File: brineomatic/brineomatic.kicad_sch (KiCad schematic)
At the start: 7 parts, among them U1 ESP32-S3-DEVKITC

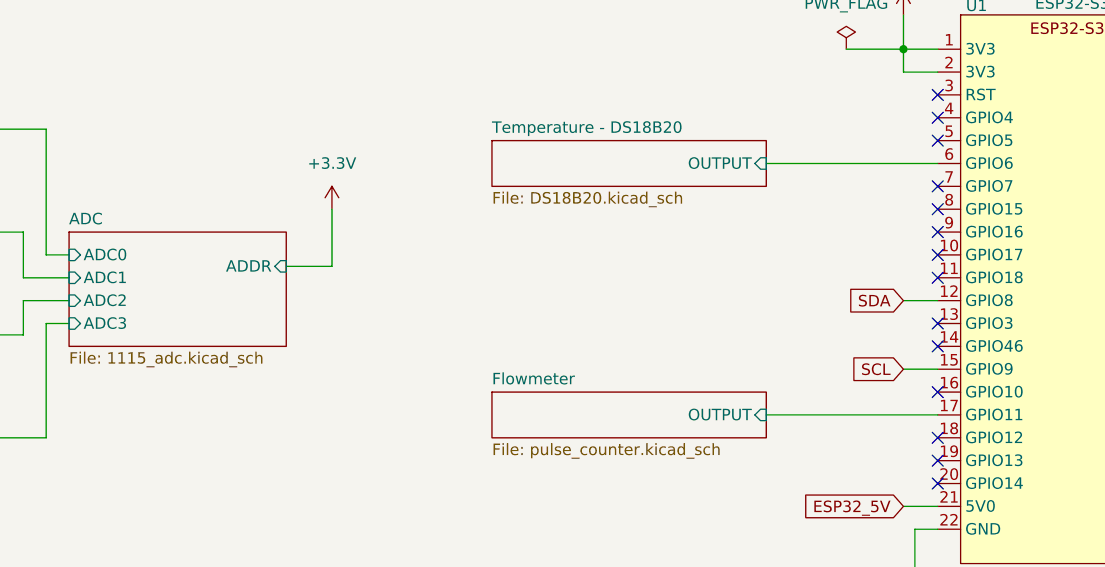
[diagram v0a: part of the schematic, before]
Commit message: added alert line to adc
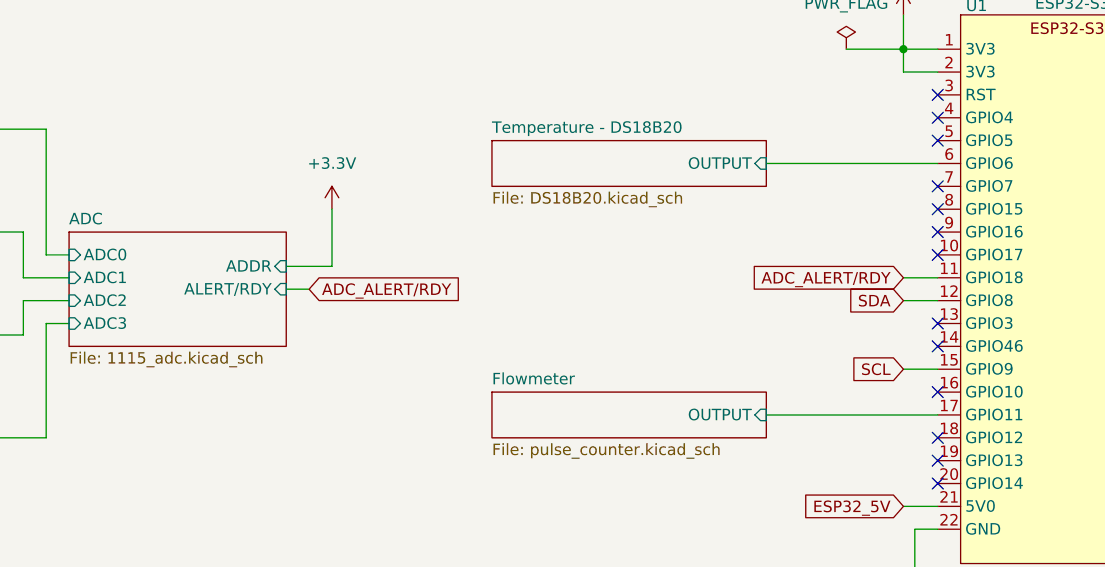
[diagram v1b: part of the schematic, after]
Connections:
- net ADC_ALERT/RDY: now reaches U1.11 (GPIO18)
- no-connect marks 25 -> 24
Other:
- sheet ADC ports: added ALERT/RDY; removed none
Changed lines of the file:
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@@
-	)
-	(no_connect
-		(at 161.29 76.2)
 	)
 	(no_connect
@@
 	(wire
 		(pts
+			(xy 88.9 77.47) (xy 91.44 77.47)
+		)
+		(stroke
+			(width 0)
+			(type default)
+		)
+	)
+	(wire
+		(pts
 			(xy 199.39 68.58) (xy 222.25 68.58)
 		)
@@
 	(wire
 		(pts
+			(xy 157.48 76.2) (xy 161.29 76.2)
+		)
+		(stroke
+			(width 0)
+			(type default)
+		)
+	)
+	(wire
+		(pts
 			(xy 207.01 50.8) (xy 207.01 52.07)
 		)
@@
 			(width 0)
 			(type default)
+		)
+	)
+	(global_label "ADC_ALERT{slash}RDY"
+		(shape input)
+		(at 157.48 76.2 180)
+		(fields_autoplaced yes)
+		(effects
+			(font
+				(size 1.27 1.27)
+			)
+			(justify right)
+		)
+		(property "Intersheetrefs" "${INTERSHEET_REFS}"
+			(at 139.4362 76.2 0)
+			(effects
+				(font
+					(size 1.27 1.27)
+				)
+				(justify right)
+				(hide yes)
+			)
 		)
 	)
@@
 				)
 				(justify right)
+				(hide yes)
+			)
+		)
+	)
+	(global_label "ADC_ALERT{slash}RDY"
+		(shape input)
+		(at 91.44 77.47 0)
+		(fields_autoplaced yes)
+		(effects
+			(font
+				(size 1.27 1.27)
+			)
+			(justify left)
+		)
+		(property "Intersheetrefs" "${INTERSHEET_REFS}"
+			(at 109.4838 77.47 0)
+			(effects
+				(font
+					(size 1.27 1.27)
+				)
+				(justify left)
 				(hide yes)
 			)
@@
 			(effects
 				(font
+					(size 1.27 1.27)
+				)
+				(justify right)
+			)
+		)
+		(pin "ALERT{slash}RDY" input
+			(at 88.9 77.47 0)
+			(effects
+				(font

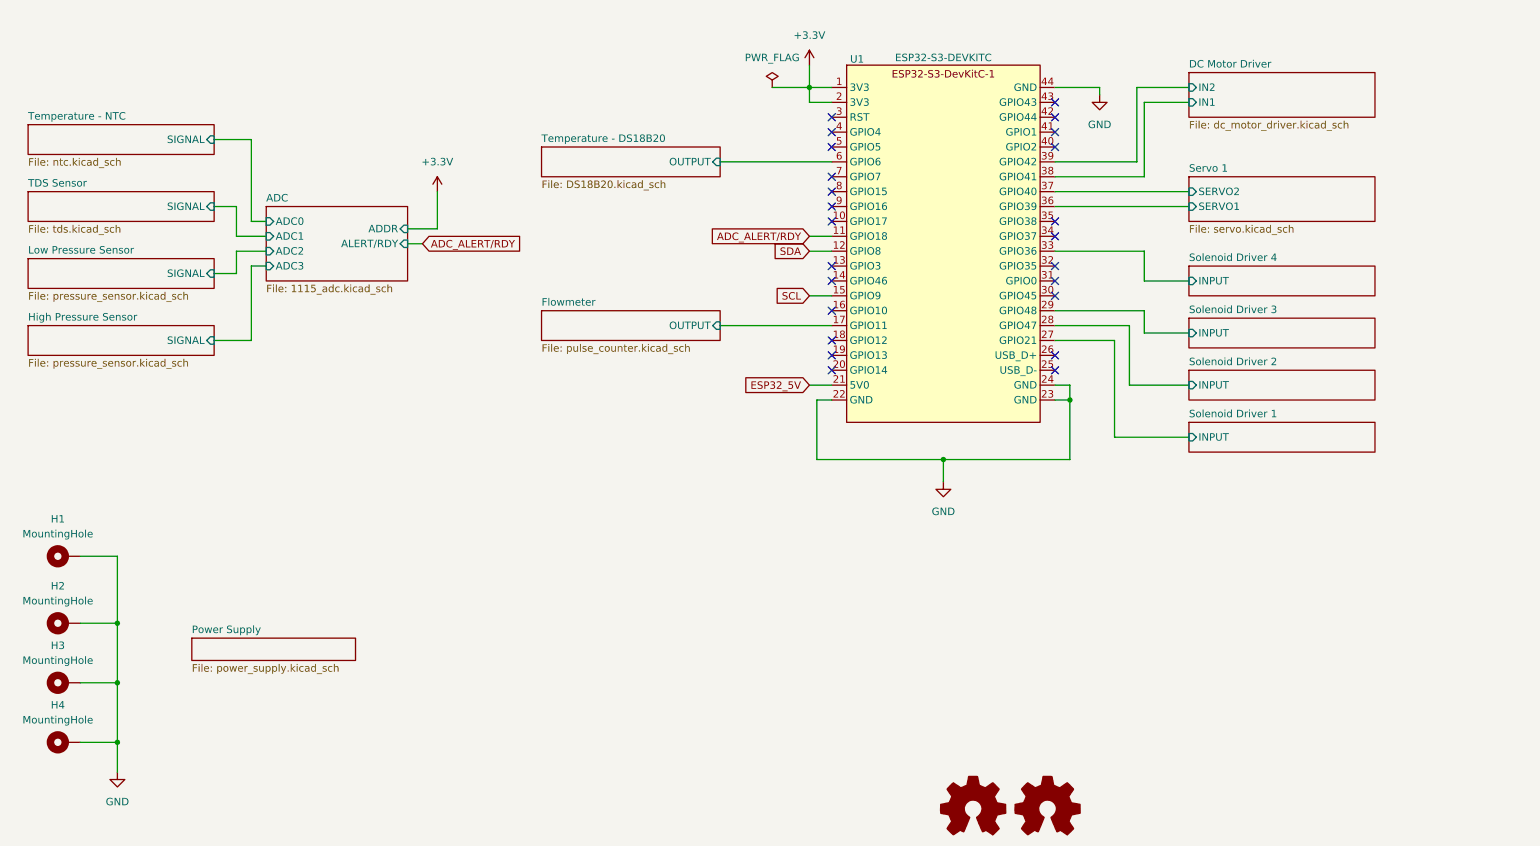
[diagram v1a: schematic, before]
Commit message: added piezo buzzer
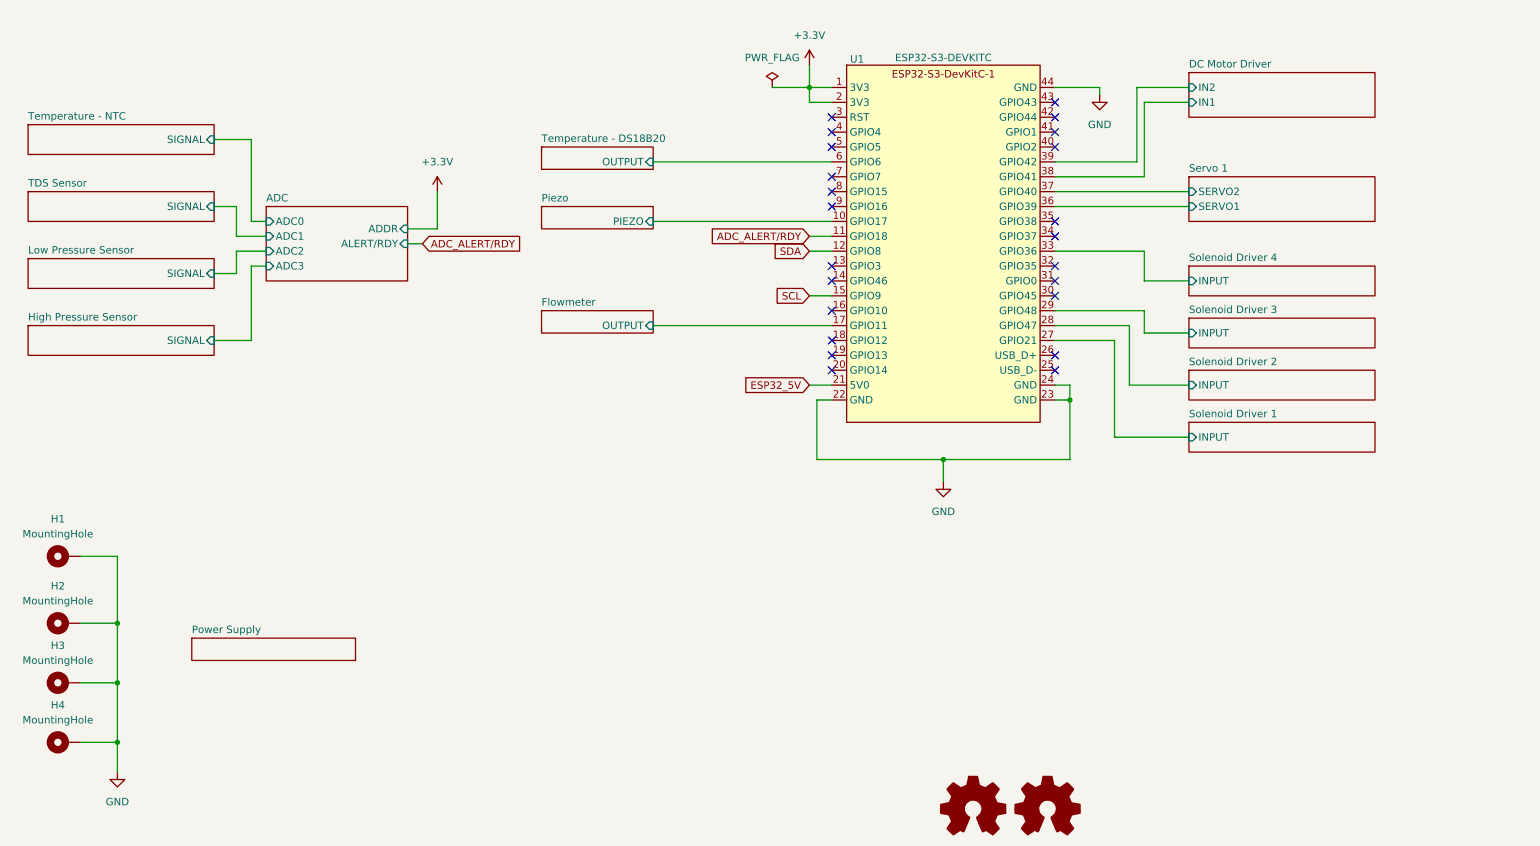
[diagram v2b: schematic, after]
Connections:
- net Piezo/PIEZO: now reaches U1.10 (GPIO17)
- no-connect marks 24 -> 23
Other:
- added sheet Piezo (piezo.kicad_sch)
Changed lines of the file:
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@@
-	)
-	(no_connect
-		(at 161.29 73.66)
 	)
 	(no_connect
@@
 	(wire
 		(pts
+			(xy 130.81 63.5) (xy 161.29 63.5)
+		)
+		(stroke
+			(width 0)
+			(type default)
+		)
+	)
+	(wire
+		(pts
 			(xy 39.37 162.56) (xy 39.37 167.64)
 		)
@@
 	(wire
 		(pts
-			(xy 161.29 91.44) (xy 142.24 91.44)
-		)
-		(stroke
-			(width 0)
-			(type default)
-		)
-	)
-	(wire
-		(pts
 			(xy 158.75 114.3) (xy 180.34 114.3)
 		)
@@
 	(wire
 		(pts
+			(xy 130.81 73.66) (xy 161.29 73.66)
+		)
+		(stroke
+			(width 0)
+			(type default)
+		)
+	)
+	(wire
+		(pts
 			(xy 180.34 118.11) (xy 180.34 114.3)
 		)
@@
 	(wire
 		(pts
-			(xy 142.24 63.5) (xy 161.29 63.5)
-		)
-		(stroke
-			(width 0)
-			(type default)
-		)
-	)
-	(wire
-		(pts
 			(xy 157.48 50.8) (xy 157.48 53.34)
 		)
@@
 		(pts
 			(xy 180.34 114.3) (xy 201.93 114.3)
+		)
+		(stroke
+			(width 0)
+			(type default)
+		)
+	)
+	(wire
+		(pts
+			(xy 130.81 91.44) (xy 161.29 91.44)
 		)
 		(stroke
@@
 				)
 				(justify left top)
+				(hide yes)
 			)
 		)
@@
 				)
 				(justify left top)
+				(hide yes)
 			)
 		)
@@
 				)
 				(justify left top)
+				(hide yes)
 			)
 		)
@@
 				)
 				(justify left top)
+				(hide yes)
 			)
 		)
@@
 				)
 				(justify left top)
+				(hide yes)
 			)
 		)
@@
 	(sheet
 		(at 111.76 60.96)
-		(size 30.48 5.08)
+		(size 19.05 3.81)
 		(fields_autoplaced yes)
 		(stroke
@@
 		)
 		(property "Sheetfile" "DS18B20.kicad_sch"
-			(at 111.76 66.6246 0)
+			(at 111.76 65.3546 0)
 			(effects
 				(font
@@
 				)
 				(justify left top)
+				(hide yes)
 			)
 		)
 		(pin "OUTPUT" input
-			(at 142.24 63.5 0)
+			(at 130.81 63.5 0)
 			(effects
 				(font
@@
 				(path "/96477ae2-ef08-48f3-8dd4-fe4478541f68"
 					(page "4")
+				)
+			)
+		)
+	)
+	(sheet
+		(at 111.76 71.12)
+		(size 19.05 3.81)
+		(fields_autoplaced yes)
+		(stroke
+			(width 0.1524)
+			(type solid)
+		)
+		(fill
+			(color 0 0 0 0.0000)
+		)
+		(property "Sheetname" "Piezo"
+			(at 111.76 70.4084 0)
+			(effects
+				(font
+					(size 1.27 1.27)
+				)
+				(justify left bottom)
+			)
+		)
+		(property "Sheetfile" "piezo.kicad_sch"
+			(at 111.76 75.5146 0)
+			(effects
+				(font
+					(size 1.27 1.27)
+				)
+				(justify left top)
+				(hide yes)
+			)
+		)
+		(pin "PIEZO" input
+			(at 130.81 73.66 0)
+			(effects
+				(font
+					(size 1.27 1.27)
+				)
+				(justify right)
+			)
+		)
+		(instances
+			(project "brineomatic"
+				(path "/96477ae2-ef08-48f3-8dd4-fe4478541f68"
+					(page "16")
 				)
 			)
@@
 				)
 				(justify left top)
+				(hide yes)
 			)
 		)
@@
 	(sheet
 		(at 111.76 88.9)
-		(size 30.48 5.08)
+		(size 19.05 3.81)
 		(fields_autoplaced yes)
 		(stroke
@@
 		)
 		(property "Sheetfile" "pulse_counter.kicad_sch"
-			(at 111.76 94.5646 0)
+			(at 111.76 93.2946 0)
 			(effects
 				(font
@@
 				)
 				(justify left top)
+				(hide yes)
 			)
 		)
 		(pin "OUTPUT" input
-			(at 142.24 91.44 0)
+			(at 130.81 91.44 0)
 			(effects
 				(font
@@
 				)
 				(justify left top)
+				(hide yes)
 			)
 		)
@@
 				)
 				(justify left top)
-			)
-		)
+				(hide yes)
+			)
+		)

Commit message: did a bunch of schematic work for Rev B
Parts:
- added R17, R19: 10k, symbol Device:R_Small_US
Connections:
- net +3.3V: now also R17.2
- net GND: now also R19.2
- net Servos/SERVO1: now also U1.34 (GPIO37); no longer U1.36 (GPIO39)
- net Servos/SERVO2: now also U1.36 (GPIO39); no longer U1.37 (GPIO40)
- net Brine Flowmeter/OUTPUT: now reaches U1.18 (GPIO12)
- net Stepper Driver/DIR: now reaches U1.40 (GPIO2)
- net Stepper Driver/STEP: now reaches U1.41 (GPIO1)
- net DC Motor Driver/IN1 renamed Stepper Driver/RX
- net DC Motor Driver/IN2 renamed Stepper Driver/EN
- new net Stepper Driver/MS1: R17.1
- new net Stepper Driver/MS2: R19.1
- new net Stepper Driver/TX: U1.37 (GPIO40)
- no-connect marks 23 -> 19
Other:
- sheet Flowmeter renamed Product Flowmeter
- sheet Servo 1 renamed Servos
- sheet TDS Sensor renamed Product TDS
- removed sheet DC Motor Driver
- removed sheet Temperature - NTC
- added sheet Brine Flowmeter (pulse_counter.kicad_sch)
- added sheet Brine TDS (tds.kicad_sch)
- added sheet Stepper Driver (tmc2209.kicad_sch)

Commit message: worked on schematic and layout a bit more.
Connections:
- net Stepper Driver/TX is gone; now on net Stepper Driver/RX: U1.37 (GPIO40)
- net Stepper Driver/RX: no longer U1.38 (GPIO41)
- new net Stepper Driver/DIAG: U1.38 (GPIO41)
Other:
- sheet Stepper Driver ports: added DIAG; removed none
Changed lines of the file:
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@@
 	(paper "A4")
+	(junction
+		(at 219.71 57.15)
+		(diameter 0)
+		(color 0 0 0 0)
+	)
 	(junction
 		(at 39.37 142.24)
@@
 	(wire
 		(pts
-			(xy 209.55 44.45) (xy 222.25 44.45)
+			(xy 209.55 43.18) (xy 222.25 43.18)
 		)
 		(stroke
@@
 	(wire
 		(pts
-			(xy 217.17 73.66) (xy 222.25 73.66)
+			(xy 217.17 74.93) (xy 222.25 74.93)
 		)
 		(stroke
@@
 	(wire
 		(pts
+			(xy 222.25 54.61) (xy 219.71 54.61)
+		)
+		(stroke
+			(width 0)
+			(type default)
+		)
+	)
+	(wire
+		(pts
 			(xy 254 44.45) (xy 257.81 44.45)
 		)
@@
 	(wire
 		(pts
-			(xy 199.39 71.12) (xy 222.25 71.12)
+			(xy 217.17 72.39) (xy 222.25 72.39)
 		)
 		(stroke
@@
 	(wire
 		(pts
-			(xy 214.63 63.5) (xy 214.63 49.53)
+			(xy 214.63 63.5) (xy 214.63 48.26)
 		)
 		(stroke
@@
 	(wire
 		(pts
-			(xy 214.63 49.53) (xy 222.25 49.53)
+			(xy 214.63 48.26) (xy 222.25 48.26)
 		)
 		(stroke
@@
 	(wire
 		(pts
-			(xy 217.17 76.2) (xy 217.17 73.66)
+			(xy 217.17 76.2) (xy 217.17 74.93)
 		)
 		(stroke
@@
 	(wire
 		(pts
-			(xy 212.09 46.99) (xy 222.25 46.99)
+			(xy 212.09 45.72) (xy 222.25 45.72)
 		)
 		(stroke
@@
 	(wire
 		(pts
+			(xy 217.17 72.39) (xy 217.17 71.12)
+		)
+		(stroke
+			(width 0)
+			(type default)
+		)
+	)
+	(wire
+		(pts
 			(xy 209.55 93.98) (xy 209.55 110.49)
 		)
@@
 	(wire
 		(pts
-			(xy 209.55 58.42) (xy 209.55 44.45)
+			(xy 217.17 52.07) (xy 222.25 52.07)
+		)
+		(stroke
+			(width 0)
+			(type default)
+		)
+	)
+	(wire
+		(pts
+			(xy 209.55 58.42) (xy 209.55 43.18)
 		)
 		(stroke
@@
 	(wire
 		(pts
-			(xy 217.17 66.04) (xy 217.17 54.61)
+			(xy 217.17 52.07) (xy 217.17 66.04)
 		)
 		(stroke
@@
 	(wire
 		(pts
-			(xy 217.17 54.61) (xy 222.25 54.61)
-		)
-		(stroke
-			(width 0)
-			(type default)
-		)
-	)
-	(wire
-		(pts
 			(xy 180.34 114.3) (xy 201.93 114.3)
 		)
@@
 	(wire
 		(pts
-			(xy 212.09 60.96) (xy 212.09 46.99)
+			(xy 212.09 60.96) (xy 212.09 45.72)
 		)
 		(stroke
@@
 	(wire
 		(pts
+			(xy 217.17 71.12) (xy 199.39 71.12)
+		)
+		(stroke
+			(width 0)
+			(type default)
+		)
+	)
+	(wire
+		(pts
 			(xy 199.39 68.58) (xy 219.71 68.58)
 		)
@@
 		(pts
 			(xy 204.47 50.8) (xy 204.47 52.07)
+		)
+		(stroke
+			(width 0)
+			(type default)
+		)
+	)
+	(wire
+		(pts
+			(xy 219.71 54.61) (xy 219.71 57.15)
 		)
 		(stroke
@@
 	)
 	(sheet
-		(at 222.25 68.58)
+		(at 222.25 69.85)
 		(size 31.75 7.62)
 		(exclude_from_sim no)
@@
 		)
 		(property "Sheetname" "Servos"
-			(at 222.25 67.8684 0)
+			(at 222.25 69.1384 0)
 			(effects
 				(font
@@
 		)
 		(property "Sheetfile" "servo.kicad_sch"
-			(at 222.25 76.7846 0)
+			(at 222.25 78.0546 0)
 			(effects
 				(font
@@
 		)
 		(property "Field2" ""
-			(at 222.25 68.58 0)
+			(at 222.25 69.85 0)
 			(effects
 				(font
@@
 		)
 		(pin "SERVO1" input
-			(at 222.25 73.66 180)
+			(at 222.25 74.93 180)
 			(effects
 				(font
@@
 		)
 		(pin "SERVO2" input
-			(at 222.25 71.12 180)
+			(at 222.25 72.39 180)
 			(effects
 				(font
@@
 		)
 		(pin "DIR" input
-			(at 222.25 46.99 180)
+			(at 222.25 45.72 180)
 			(effects
 				(font
@@
 		)
 		(pin "EN" input
-			(at 222.25 49.53 180)
+			(at 222.25 48.26 180)
 			(effects
 				(font
@@
 		)
 		(pin "STEP" input
-			(at 222.25 44.45 180)
+			(at 222.25 43.18 180)
 			(effects
 				(font
@@
 			)
 		)
+		(pin "DIAG" input
+			(at 222.25 52.07 180)
+			(effects
+				(font
+					(size 1.27 1.27)
+				)
+				(justify left)
+			)
+		)

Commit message: lots of progress on Rev B
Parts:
- R17, R19: footprint (none) -> Resistor_SMD:R_0603_1608Metric
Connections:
- net ADC_ALERT/RDY: now also U1.7 (GPIO7); no longer U1.11 (GPIO18)
- net Brine Flowmeter/OUTPUT: now also U1.17 (GPIO11); no longer U1.18 (GPIO12)
- net Product Flowmeter/OUTPUT: now also U1.18 (GPIO12); no longer U1.17 (GPIO11)
- net TMC2209_RX: now reaches U1.8 (GPIO15)
- no-connect marks 19 -> 17
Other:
- moved on the sheet: R17, R19
